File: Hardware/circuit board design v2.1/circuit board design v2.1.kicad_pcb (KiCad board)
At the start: 4 copper layers, 28.1 x 76.1 mm, 60 parts, among them J1 Conn_01x02_Male, J2 Conn_01x02, J3 105017-0001, J4 U.FL-R-SMT-1_10_, J6 Conn_01x02_Male, U1 STM32F446RETx, U10 LAMBDA-9D, U11 2SCR512R_HZG, U12 L80-R, U2 W25Q64JVSS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

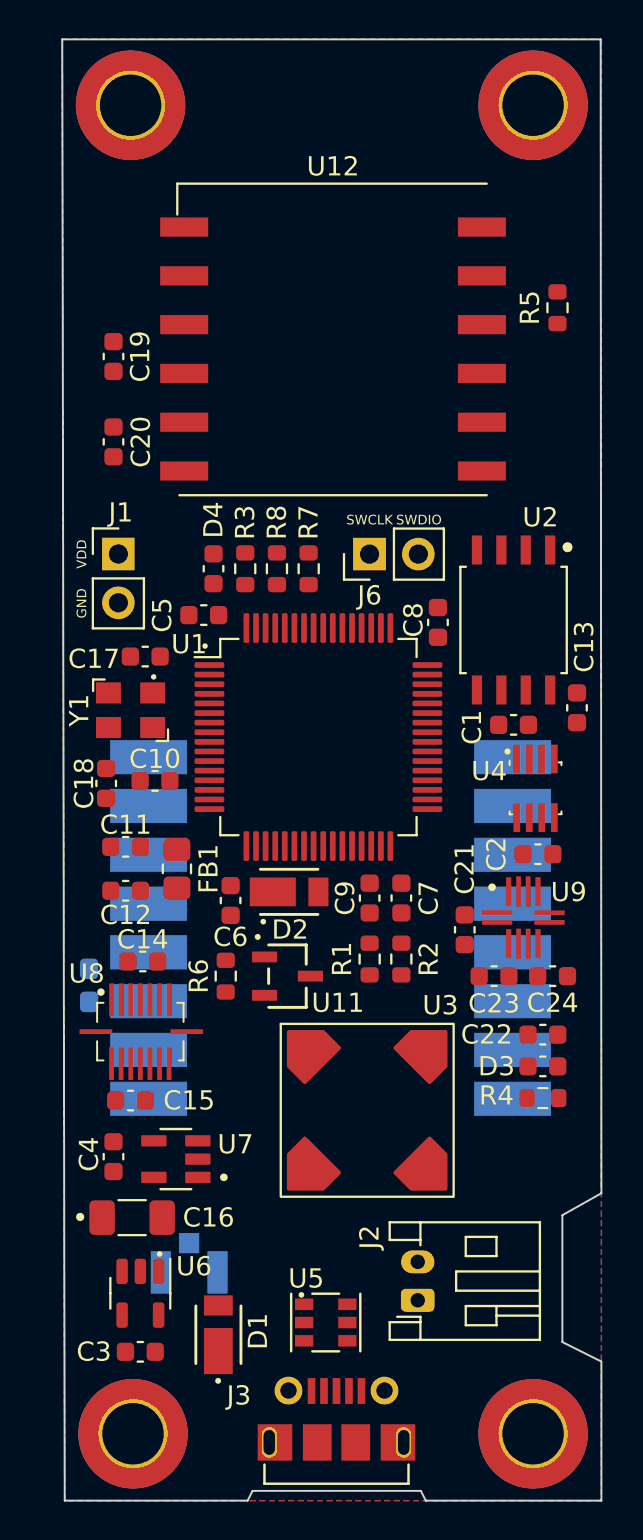
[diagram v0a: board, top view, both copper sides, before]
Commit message: Found error transistor pinout
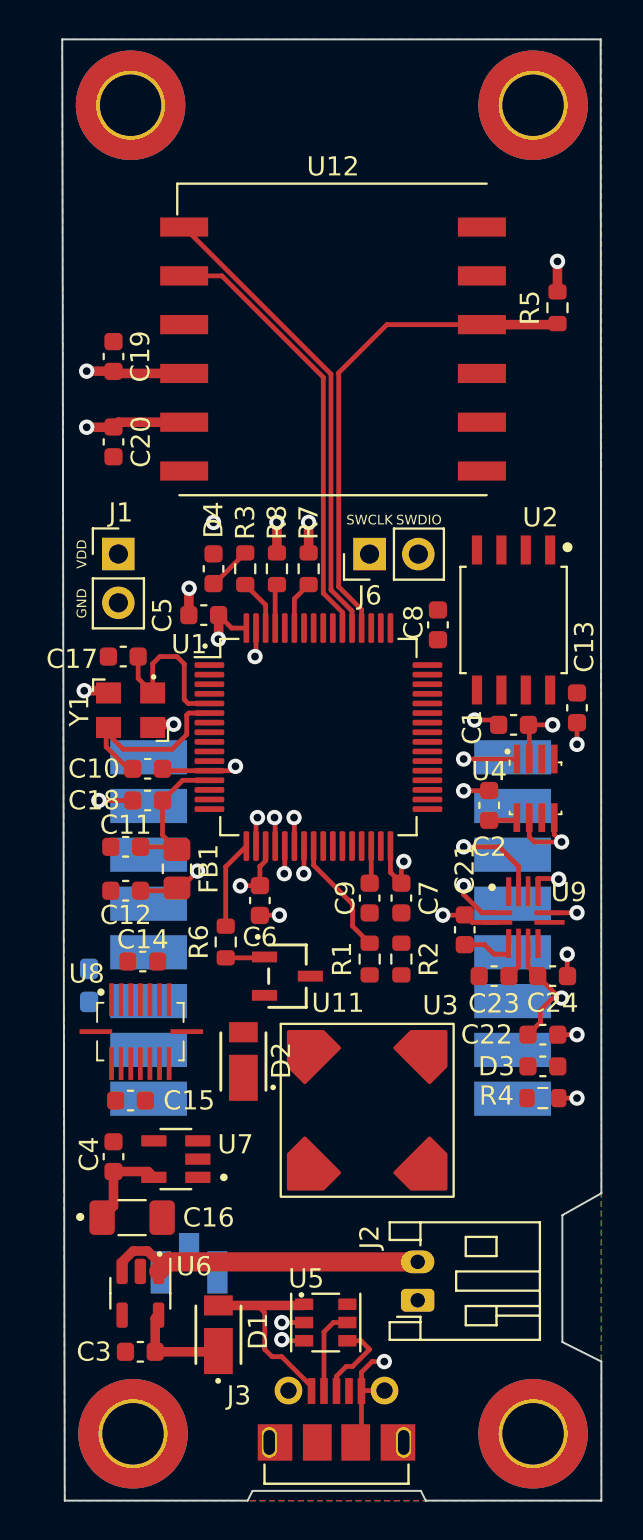
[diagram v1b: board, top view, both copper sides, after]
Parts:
- R6: value R_0603 -> 3.3k
- moved D2 9.15 mm to (31.4, 71.1), turned to -90 degrees
- moved C2 3.59 mm to (44.2, 57.8), turned to 90 degrees
- moved C18 2.29 mm to (26.4, 55.9), turned to 0 degrees
- moved R6 1.78 mm to (30.5, 64.9)
- moved C6 1.52 mm to (32.3, 62.7)
- moved C17 1.14 mm to (25.1, 50.0)
- moved C10 1.09 mm to (26.4, 57.5)
- moved C8 0.13 mm to (41.5, 48.4)
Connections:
- net Net-(U1-Pad5) renamed /MCU/OSCI+
- net Net-(U1-Pad6) renamed /MCU/OSCI-
- R6 pad 2: Net-(U11-Pad2) -> Net-(R6-Pad2)
- U1 pad 52: unconnected-(U1-Pad52) -> /GPS/reset_gps
- U1 pad 55: /GPS/reset_gps -> unconnected-(U1-Pad55)
- U11 pad 1: GND -> Net-(R6-Pad2)
- U11 pad 2: Net-(U11-Pad2) -> GND
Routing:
- net +3.3V: track 0.00 -> 45.2 mm, vias 0 -> 13
- net GND: track 0.00 -> 44.6 mm, vias 0 -> 21
- net /GPS/reset_gps: track 0.00 -> 26.2 mm
- net /GPS/rx_gps: track 0.00 -> 24.5 mm
- net /GPS/tx_gps: track 0.00 -> 22.9 mm
- net /Power/Battery+: track 0.00 -> 17.1 mm
- net VBUS: track 0.00 -> 12.4 mm
- net +3.3VA: track 0.00 -> 11.1 mm
- net /MCU/OSCI-: track 0.00 -> 10.2 mm
- net /MCU/OSCI+: track 0.00 -> 8.93 mm
- net /MCU/PWR_BVOLTS: track 0.00 -> 6.27 mm
- net Net-(D1-Pad1): track 0.00 -> 5.29 mm
- net /MCU/buzzer_gate: track 0.00 -> 4.61 mm
- net /Power/D-: track 0.00 -> 4.49 mm
- net /Power/D+: track 0.00 -> 4.42 mm
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
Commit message: Renamed pins in stm32cubeide and finished routing for V2.1
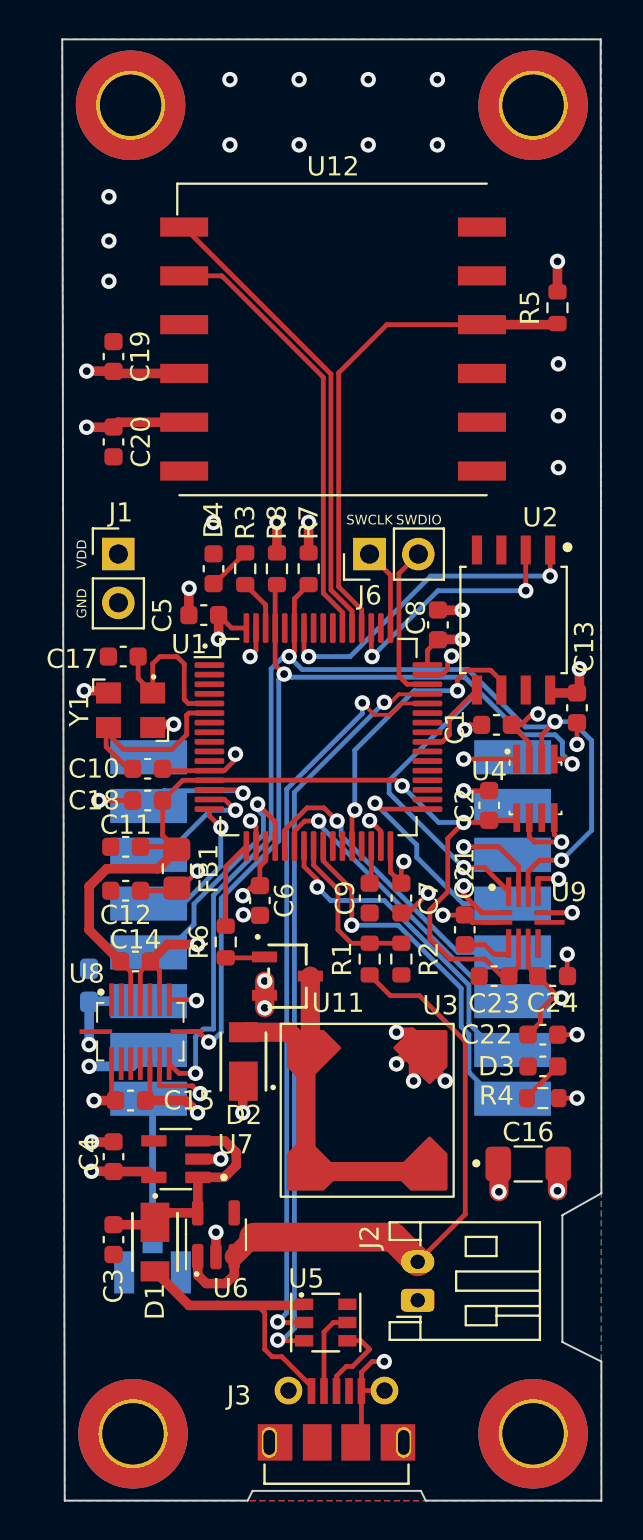
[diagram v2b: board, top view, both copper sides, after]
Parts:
- R3, R4: value R_0603 -> 330
- moved C16 20.8 mm to (46.2, 76.5)
- moved C3 6.01 mm to (24.6, 80.4), turned to -90 degrees
- moved D1 5.85 mm to (26.8, 80.5), turned to 90 degrees
- moved U6 4.98 mm to (30.0, 80.1), turned to 90 degrees
- moved J4 1.90 mm to (26.7, 82.1)
- moved C1 0.89 mm to (44.6, 53.6)
- moved C14 0.38 mm to (25.8, 65.9)
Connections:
- net /GPS/reset_gps renamed /GPS/GPS_Reset
- net /GPS/rx_gps renamed /GPS/GPS_UART_RX_Module
- net /GPS/tx_gps renamed /GPS/GPS_UART_TX_Module
- net /MCU/PWR_BVOLTS renamed /MCU/Battery_Voltage
- net /MCU/QUADSPI_CLK renamed /MCU/Flash_QUADSPI_CLK
- net /MCU/QUADSPI_IO0 renamed /MCU/Flash_QUADSPI_BK1_IO0
- net /MCU/QUADSPI_IO1 renamed /MCU/Flash_QUADSPI_BK1_IO1
- net /MCU/QUADSPI_NCS renamed /MCU/Flash_QUADSPI_BK1_NCS
- net /MCU/SPI1_MISO renamed /MCU/Radio_SPI1_MISO
- net /MCU/SPI1_MOSI renamed /MCU/Radio_SPI1_MOSI
- net /MCU/SPI1_SCK renamed /MCU/Radio_SPI1_SCK
- net /MCU/buzzer_gate renamed /MCU/Buzzer_Gate
- net /MCU/usb_d+ renamed /MCU/USB_D+
- net /MCU/usb_d- renamed /MCU/USB_D-
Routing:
- net /MCU/SCL: track 2.30 -> 61.1 mm, vias 0 -> 4
- net /MCU/SDA: track 2.57 -> 59.9 mm, vias 0 -> 4
- net +3.3VA: track 11.1 -> 50.5 mm, vias 0 -> 2
- net /MCU/USB_D+: track 1.19 -> 39.5 mm, vias 1 -> 2
- net /MCU/USB_D-: track 1.16 -> 39.3 mm, vias 1 -> 2
- net GND: track 44.6 -> 74.6 mm, vias 21 -> 49
- net +3.3V: track 45.2 -> 73.0 mm, vias 13 -> 25
- net Net-(D2-Pad2): track 0.00 -> 20.3 mm
- net /MCU/Radio_Enable: track 0.00 -> 19.2 mm, vias 0 -> 1
- net /MCU/Flash_QUADSPI_BK1_NCS: track 0.00 -> 17.3 mm, vias 0 -> 2
- net /Power/Battery+: track 17.1 -> 33.6 mm
- net /MCU/Radio_SPI1_MOSI: track 1.44 -> 17.3 mm
- net /MCU/Flash_QUADSPI_CLK: track 0.00 -> 15.5 mm, vias 0 -> 2
- net /MCU/Radio_SPI1_SCK: track 1.45 -> 16.6 mm
- net /MCU/Radio_SPI1_MISO: track 1.49 -> 16.3 mm
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
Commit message: Added interupt pins to from BMI088 and LIS
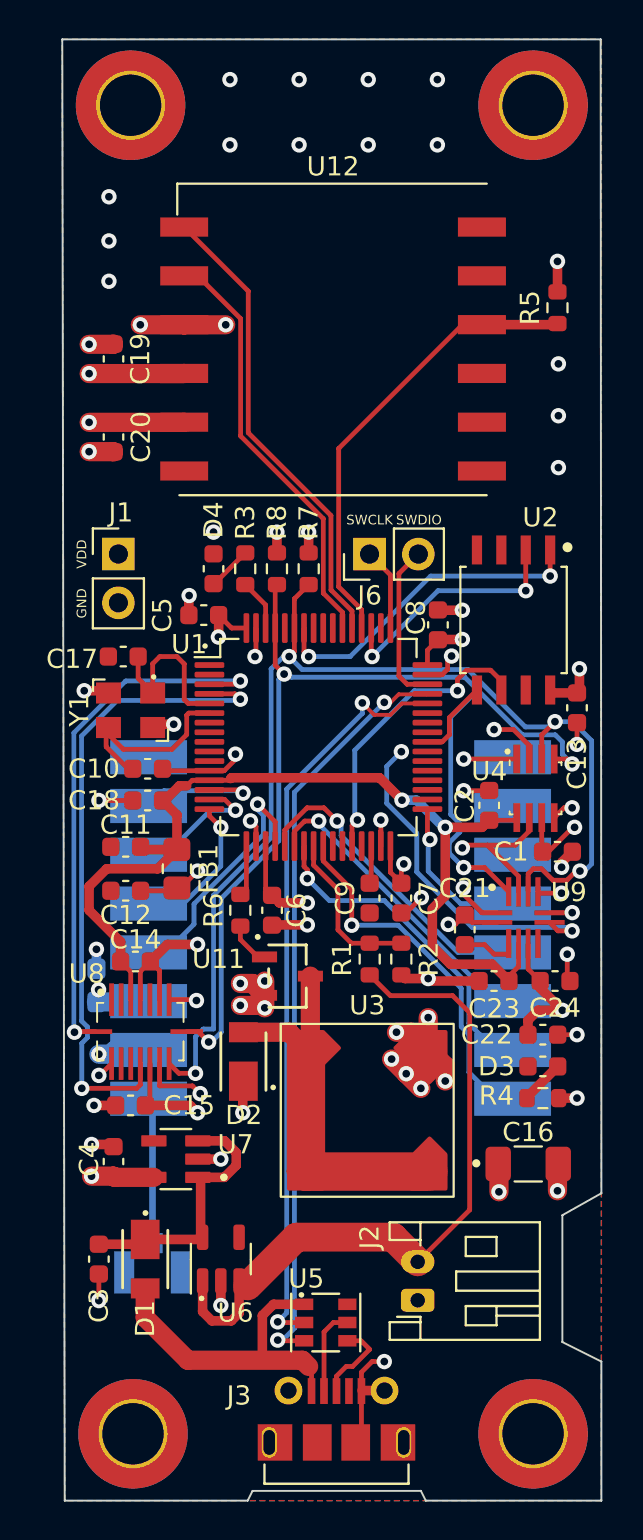
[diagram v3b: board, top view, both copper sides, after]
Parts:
- added L1: Logo, Components:ICSS_Logo, B.Cu at (35.8, 29.7)
- moved C1 7.33 mm to (47.8, 60.2), turned to 0 degrees
- moved R6 1.82 mm to (31.2, 63.2)
- moved U6 1.30 mm to (30.2, 81.4)
- moved C3 1.27 mm to (23.9, 81.4)
- moved D1 1.02 mm to (26.3, 81.4)
- moved C6 0.81 mm to (32.9, 63.2)
- moved C27 0.38 mm to (23.7, 67.2)
- moved C24 0.28 mm to (47.6, 66.9)
- moved C15 0.25 mm to (25.5, 73.4)
- moved C20 0.25 mm to (24.6, 38.6)
- moved C23 0.25 mm to (44.5, 66.9)
- moved C4 0.25 mm to (24.6, 76.3)
- moved C19 0.13 mm to (24.6, 34.5)
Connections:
- net /MCU/SCL renamed /MCU/I2C1_SCL
- net /MCU/SDA renamed /MCU/I2C1_SDA
- U1 pad 3: unconnected-(U1-Pad3) -> /MCU/Acc_Int1
- U1 pad 39: unconnected-(U1-Pad39) -> /MCU/Mag_Data_Ready
- U1 pad 4: unconnected-(U1-Pad4) -> /MCU/Gyro_Int3
- U4 pad 6: unconnected-(U4-Pad6) -> +3.3V
- U8 pad 12: unconnected-(U8-Pad12) -> /MCU/Gyro_Int3
- U8 pad 16: unconnected-(U8-Pad16) -> /MCU/Acc_Int1
- U9 pad 8: unconnected-(U9-Pad8) -> /MCU/Mag_Data_Ready
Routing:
- net /MCU/Gyro_Int3: track 0.00 -> 33.6 mm, vias 0 -> 2
- net /MCU/Acc_Int1: track 0.00 -> 28.2 mm, vias 0 -> 2
- net /MCU/Mag_Data_Ready: track 0.00 -> 17.9 mm, vias 0 -> 2
- net GND: track 74.6 -> 89.3 mm, vias 49 -> 59
- net /MCU/Radio_Reset: track 12.6 -> 8.42 mm
- net +3.3V: track 73.0 -> 75.7 mm, vias 25 -> 28
- net /Power/Battery+: track 33.6 -> 36.1 mm
- net /GPS/GPS_Reset: track 26.2 -> 23.9 mm
- net /MCU/I2C1_SCL: track 61.1 -> 58.9 mm
- net Net-(C3-Pad1): track 11.7 -> 13.8 mm
- net /MCU/Buzzer_Gate: track 4.61 -> 2.65 mm
- net /MCU/I2C1_SDA: track 59.9 -> 61.4 mm
- net VBUS: track 16.5 -> 17.4 mm
- net /GPS/GPS_UART_TX_Module: track 22.9 -> 22.2 mm

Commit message: Added solder jumpers
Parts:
- added JP1: SolderJumper_2_Open, Jumper:SolderJumper-2_P1.3mm_Open_TrianglePad1.0x1.5mm, F.Cu at (28.1, 45.3)
- added JP2: SolderJumper_2_Open, Jumper:SolderJumper-2_P1.3mm_Open_TrianglePad1.0x1.5mm, F.Cu at (47.0, 74.2)
- moved R4 0.89 mm to (47.0, 72.1), turned to 180 degrees
- moved D3 0.76 mm to (47.0, 70.6)
- moved C22 0.64 mm to (47.0, 69.1), turned to 180 degrees
- moved D4 0.38 mm to (30.2, 45.5), turned to 90 degrees
- moved C16 0.25 mm to (46.2, 76.7)
- moved R3 0.25 mm to (31.8, 45.5)
- moved R8 0.13 mm to (33.3, 45.5)
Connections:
- D4 pad 1: GND -> Net-(D4-Pad1)
- R4 pad 2: +3.3V -> Net-(R4-Pad2)
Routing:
- net Net-(D4-Pad1): track 0.00 -> 2.23 mm
- net Net-(R4-Pad2): track 0.00 -> 2.12 mm
- net /MCU/Mag_Data_Ready: track 17.9 -> 19.6 mm
- net +3.3V: track 75.7 -> 74.2 mm
- net GND: track 89.3 -> 90.4 mm
- net Net-(D3-Pad2): track 2.31 -> 1.54 mm
- net Net-(R3-Pad2): track 2.31 -> 1.54 mm

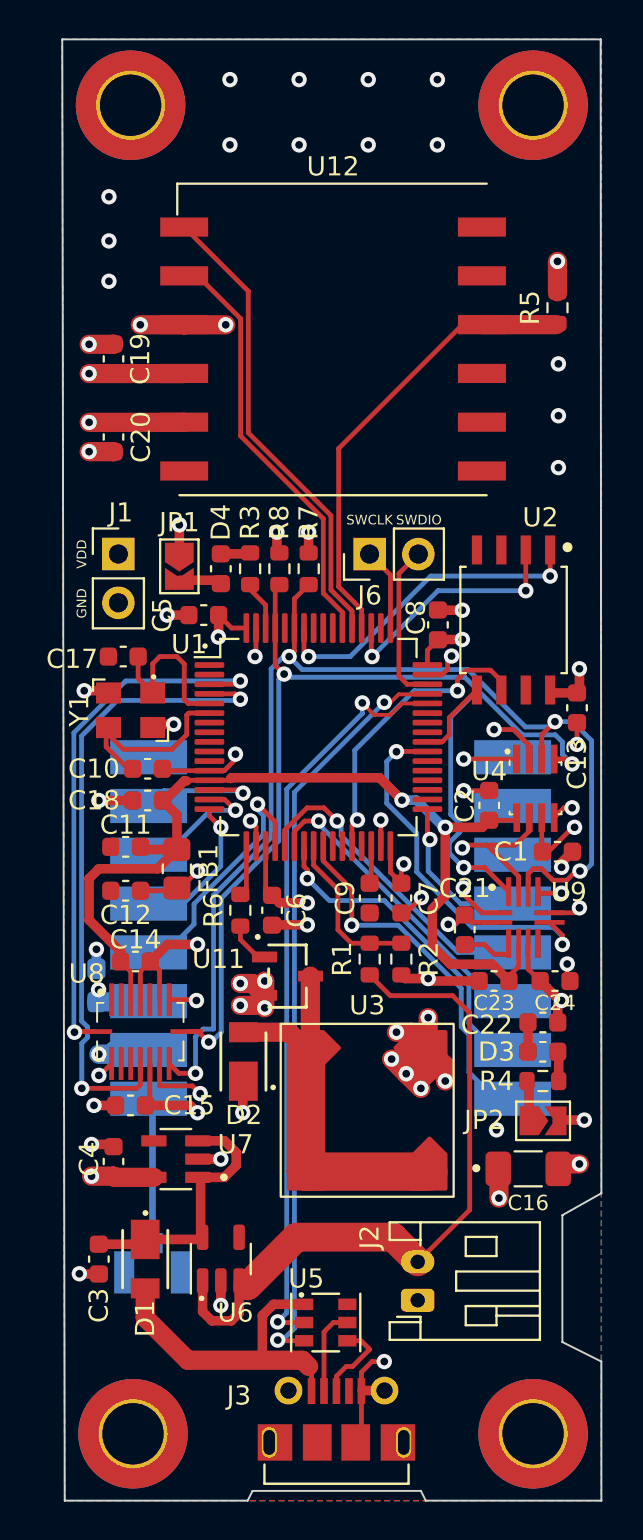
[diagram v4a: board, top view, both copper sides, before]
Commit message: PCB V2.1 sent for manufacture
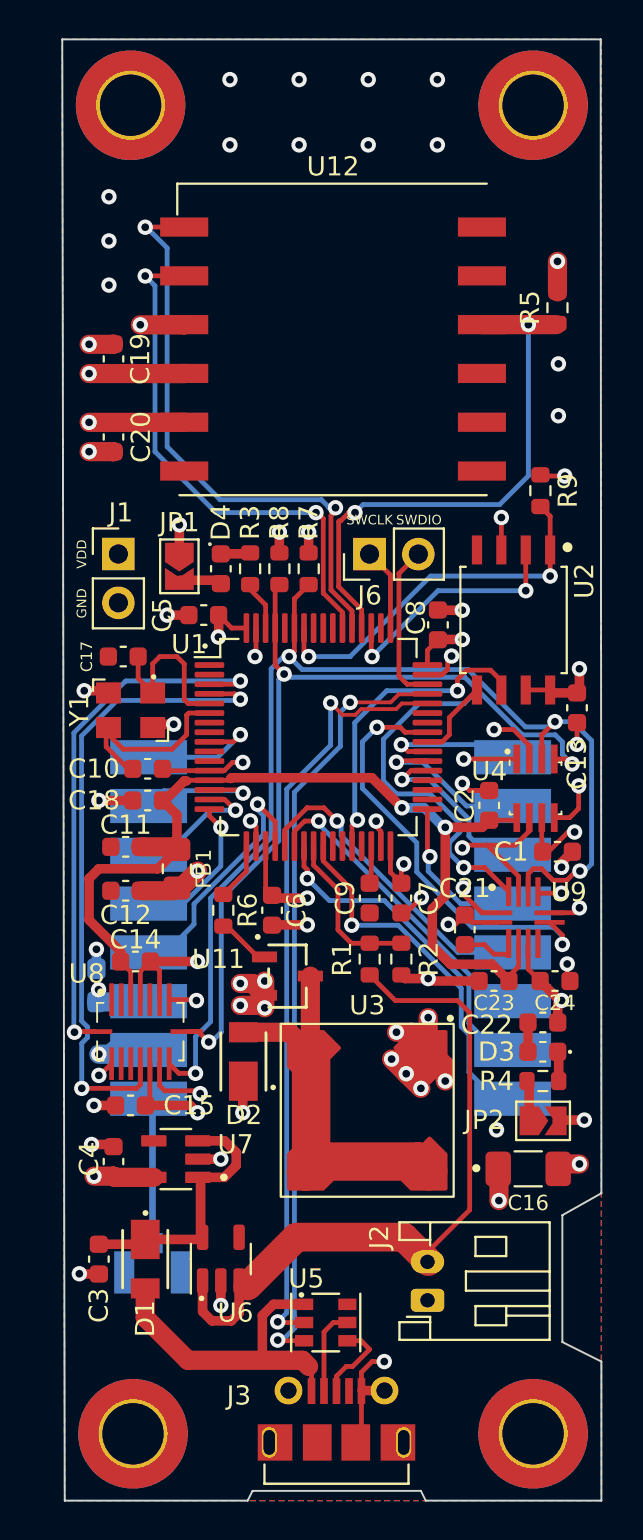
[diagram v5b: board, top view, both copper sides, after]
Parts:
- added R9: 4.7k, Components:R_0603_1608Metric, F.Cu at (46.9, 41.4)
- C16: value 4.7uF -> 4.7uF Tantalum Capacitor
- D1, D2: value DFLS130L -> DFLS130L Schottkey Diode
- D3: value LED_0603 -> SML-LX0603GW-TR Green LED
- D4: value LED_0603 -> SML-LX0603IW-TR Red LED
- FB1: value 120R@100MHz -> 742792025 Ferrite Bead 120R@100MHz
- J1, J6: value Conn_01x02_Male -> 01x02_Male_PinHeader_2.54mm
- J2: value Conn_01x02 -> JST_PH_S2B-PH-K_1x02_P2.00mm_Horizontal
- J3: value 105017-0001 -> 105017-0001 Micro USB Conn
- J4: value U.FL-R-SMT-1_10_ -> [OPTIONAL] U.FL-R-SMT-1_10_ Antenna Conn
- R3, R4: value 330 -> 100
- R7, R8: value R_0603 -> 4.7k
- U1: value STM32F446RETx -> STM32F446RET6
- U10: value LAMBDA-9D -> LAMBDA-9D Radio
- U11: value 2SCR512R_HZG -> 2SCR512R_HZG BJT
- U12: value L80-R -> L80-R GPS
- U2: value W25Q64JVSS -> W25Q64JVSS 64MBit Flash Chip
- U3: value SDR08540M3-01 -> SDR08540M3-01 SMD Buzzer
- U4: value BME280 -> BME280 Environment Sensor
- U5: value STF202-22T1G -> STF202-22T1G ESD/EMI Chip
- U6: value MAX40203_SOT23 -> MAX40203_SOT23 Ideal Diode
- U7: value NCP161ASN330T1G -> NCP161ASN330T1G LDO
- U8: value BMI088 -> BMI088 Inertial Measurement Unit
- U9: value LIS3MDLTR -> LIS3MDLTR Magnetometer
- Y1: value ECS-80-8-33Q-ADS-TR3 -> ECS-80-8-33Q-ADS-TR3 8MHz Crystal
- moved R6 0.89 mm to (30.4, 63.2)
- moved J2 0.51 mm to (41.0, 83.5)
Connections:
- U1 pad 37: unconnected-(U1-Pad37) -> /MCU/Radio_DIO5
- U1 pad 38: unconnected-(U1-Pad38) -> /MCU/Radio_DIO4
- U1 pad 39: /MCU/Mag_Data_Ready -> /MCU/Radio_DIO3
- U1 pad 41: unconnected-(U1-Pad41) -> /MCU/Mag_Data_Ready
- U1 pad 9: unconnected-(U1-Pad9) -> /MCU/Radio_DIO2
- U10 pad 10: unconnected-(U10-Pad10) -> /MCU/Radio_DIO4
- U10 pad 11: unconnected-(U10-Pad11) -> /MCU/Radio_DIO5
- U10 pad 8: unconnected-(U10-Pad8) -> /MCU/Radio_DIO2
- U10 pad 9: unconnected-(U10-Pad9) -> /MCU/Radio_DIO3
- U2 pad 3: unconnected-(U2-Pad3) -> +3.3V
- U2 pad 7: unconnected-(U2-Pad7) -> +3.3V
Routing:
- net /MCU/Radio_DIO5: track 0.00 -> 9.42 mm, vias 0 -> 1
- net /MCU/Radio_DIO4: track 0.00 -> 8.65 mm, vias 0 -> 1
- net /MCU/Radio_DIO3: track 0.00 -> 7.58 mm, vias 0 -> 1
- net /MCU/Radio_DIO2: track 0.00 -> 7.03 mm, vias 0 -> 1
- net /GPS/GPS_UART_RX_Module: track 24.5 -> 30.9 mm, vias 0 -> 2
- net /GPS/GPS_UART_TX_Module: track 22.2 -> 27.7 mm, vias 0 -> 2
- net /MCU/I2C1_SCL: track 58.9 -> 64.2 mm
- net /GPS/GPS_Reset: track 23.9 -> 28.7 mm, vias 0 -> 2
- net +3.3V: track 74.2 -> 78.3 mm, vias 28 -> 30
- net /MCU/Mag_Data_Ready: track 19.6 -> 22.6 mm
- net /MCU/Flash_QUADSPI_BK1_NCS: track 17.3 -> 19.7 mm
- net /MCU/USB_D+: track 39.5 -> 40.5 mm
- net /MCU/USB_D-: track 39.3 -> 40.3 mm
- net /MCU/Flash_QUADSPI_CLK: track 15.6 -> 16.4 mm
- net GND: track 90.4 -> 89.7 mm, vias 59 -> 57
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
